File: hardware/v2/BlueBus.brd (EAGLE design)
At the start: 95 x 65 mm, 150 parts, among them J1 TC2030, Q1 NMOSFET-BSS138K, Q2 PMOSFET-DMP32D4SSOT323, Q3 NMOSFET-BSS138K

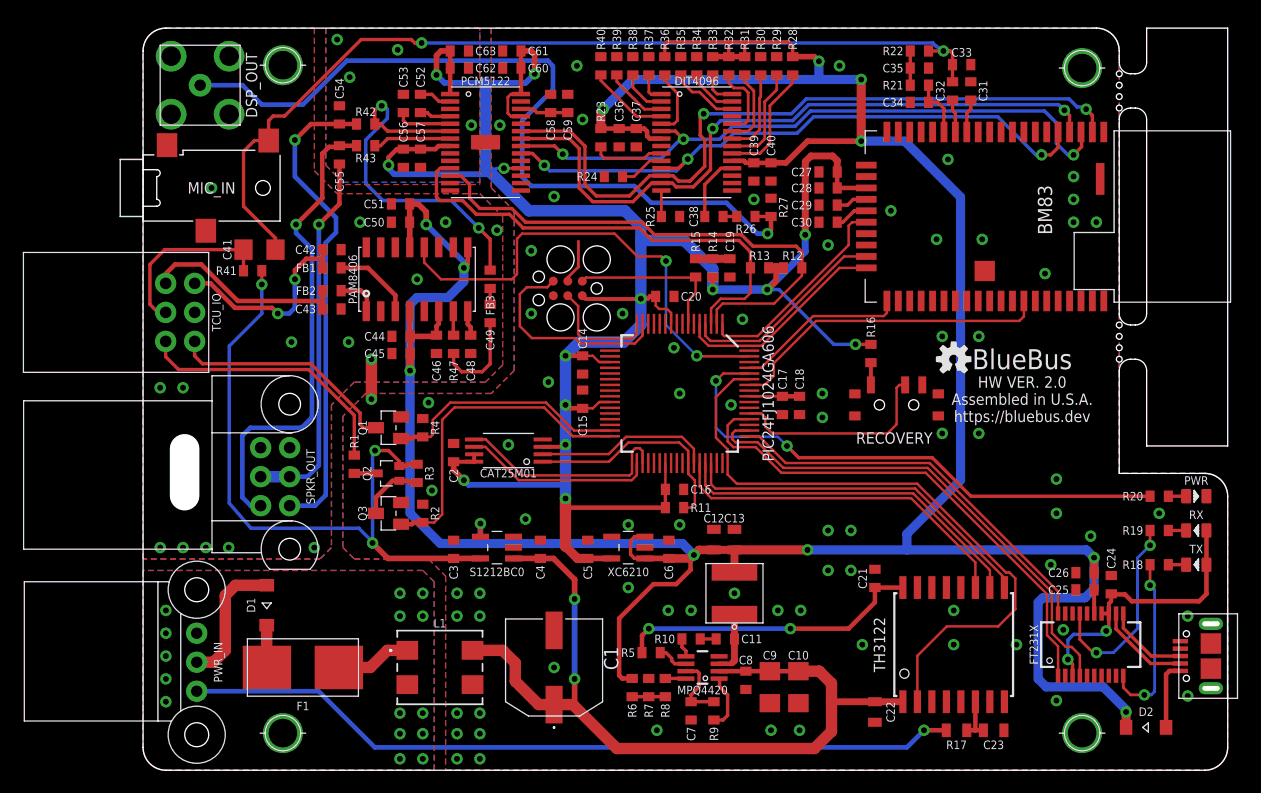
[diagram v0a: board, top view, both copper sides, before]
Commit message: [IMP] hardware: V2 Improvements * Increase the footprint for C1 and fix the name location * Remove PU/PD resistors from DIT4096 * Rewire I2S lines * Fix ground pour polygon dimensions * Replace 10ohm resistor for two parallel 20ohm * Wire SMB ground to unfiltered ground * Rename all connectors and ICs per convention * Increase name size to 1mm at minimum * Add additional ground VIAs
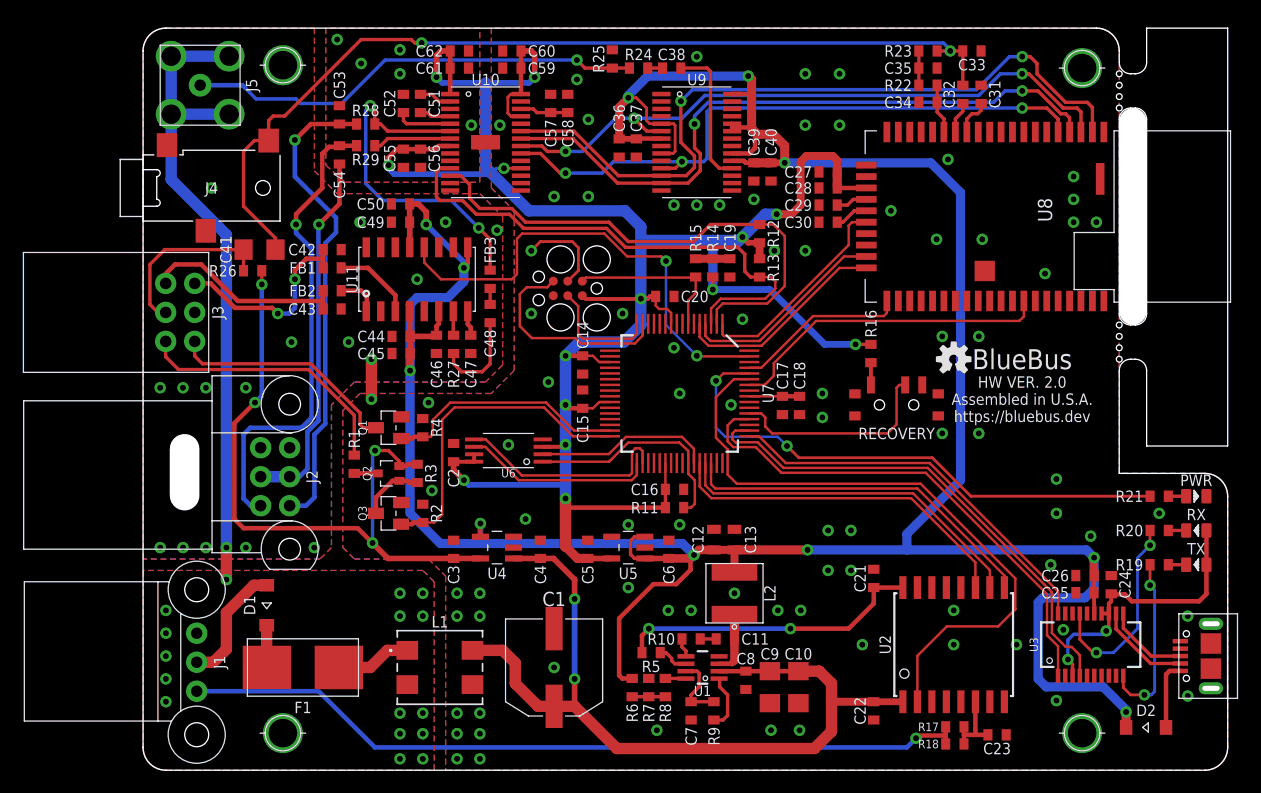
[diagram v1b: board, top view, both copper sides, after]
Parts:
- removed C63: 10uF, Passives:0603
- removed PWR_IN: 3PIN_953442_1, Connectors:TE_MQS_3PIN
- removed R30, R31, R32, R33, R34, R35, R36, R37, R38, R39, R40: 4.7k, Passives:0603
- removed R41: 10k, Passives:0603
- removed R42, R43: 100, Passives:0603
- removed R47: 18k, Passives:0603
- added C47: 1uF, Passives:0603
- added J8: TC2030, Connectors:TC2030
- C22: device Passives:0805 -> Passives:0603
- C23: value 100PF -> 100pF; device Passives:0805 -> Passives:0603
- C50: value 1uF -> 10uF
- C51: value 10uF -> 2.2uF
- C53: value 2.2uF -> 10nF
- C55: value 10nF -> 0.1uF
- C56, C60, C62: value 0.1uF -> 10uF
- C58, C61: value 10uF -> 0.1uF
- J1: value TC2030 -> 3PIN_953442_1; device Connectors:TC2030 -> Connectors:TE_MQS_3PIN
- R17: value 10 -> 20; device Passives:0805 -> Passives:0603
- R18: value 2k -> 20
- R21: value 1k -> 2k
- R23: value 4.7k -> 1k
- R24, R25: value 4.7k -> 150
- R26: value 150 -> 10k
- R27: value 150 -> 18k
- R28, R29: value 4.7k -> 100
- moved J1 44.4 mm to (4.70, 12.0), turned to 270 degrees
- moved R26 43.5 mm to (9.60, 43.8), turned to 180 degrees
- moved R21 41.7 mm to (89.0, 24.0), turned to 180 degrees
- moved R28 37.7 mm to (19.5, 56.6), turned to 180 degrees
- moved R29 36.7 mm to (19.5, 54.7), turned to 180 degrees
- moved R27 30.3 mm to (27.2, 37.3)
- moved R23 29.6 mm to (68.8, 63.0), turned to 180 degrees
- moved R18 23.8 mm to (71.1, 2.30), turned to 0 degrees
- moved R25 14.7 mm to (41.1, 62.3), turned to 90 degrees
- moved C38 13.5 mm to (46.3, 61.5), turned to 180 degrees
- moved C57 12.4 mm to (35.7, 58.4), turned to 90 degrees
- moved C49 11.2 mm to (22.6, 48.0), turned to 180 degrees
- moved R24 9.75 mm to (43.4, 61.5), turned to 180 degrees
- moved C51 8.97 mm to (24.3, 58.4), turned to 270 degrees
- moved C59 5.80 mm to (32.3, 61.5), turned to 180 degrees
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- renumbered BM83 to U8, CAT25M01 to U6, DIT4096 to U9, DSP_OUT to J5, FT231X to U3, MIC_IN to J4, MPQ4420 to U1, PAM8406 to U11, PCM5122 to U10, PIC24FJ1024GA606 to U7, RECOVERY to J7, S1212BC0 to U4, SPKR_OUT to J2, TCU_IO to J3, TH3122 to U2, USB to J6, XC6210 to U5
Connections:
- removed net SPDIF_AUDIO: R30.2, U9.22
- removed net SPDIF_BLSM: R32.1, U9.24
- removed net SPDIF_CLK0: R36.2, U9.5
- removed net SPDIF_CLK1: R40.2, U9.4
- removed net SPDIF_COPY: R38.2, U9.2
- removed net SPDIF_CSS: R37.1, U9.1
- removed net SPDIF_EMPH: R31.1, U9.23
- removed net SPDIF_FMT0: R23.2, U9.9
- removed net SPDIF_FMT1: R24.2, U9.10
- removed net SPDIF_L: R39.2, U9.3
- removed net SPDIF_MDAT: R28.1, U9.20
- removed net SPDIF_MODE: R33.2, U9.28
- removed net SPDIF_MONO: R29.1, U9.21
- removed net SPDIF_MS: R25.1, U9.14
- removed net SPDIF_U: R34.2, U9.27
- removed net SPDIF_V: R35.2, U9.26
- net 12V: now also R26.1; no longer R41.1
- net 3.3V: now also C55.1, C59.1, J8.2; no longer C57.1, C63.1, J1.2
- net 5V: now also C49.1, U9.20, U9.23, U9.24, U9.28, U9.5, U9.9; no longer C51.1, R23.1, R28.2, R31.2, R32.2, R33.1, R36.1
- net AGND: now also C52.1, C53.2, C61.2; no longer C53.1, C57.2, C63.2
- net BT_MIC_L: now also R23.1; no longer R22.1
- net DAC_CAPM: now also C51.2; no longer C52.2
- net DAC_CAPP: now also C51.1; no longer C52.1
- net DAC_LDOO: now also C57.1; no longer C59.1
- net DAC_OUT_L: now also R28.1; no longer R42.1
- net DAC_OUT_R: now also R29.1; no longer R43.1
- net DAC_VNEG: now also C52.2; no longer C53.2
- net GND: now also C47.2, C49.2, C57.2, J7.4, J7.5, J7.6, J7.7, J8.3, U9.1, U9.10, U9.14, U9.2, U9.21, U9.22, U9.26, U9.27, U9.3, U9.4; no longer C48.2, C51.2, C61.2, J1.3, J5.1, J5.2, J5.3, J5.4, R24.1, R27.2, R29.2, R30.1, R34.1, R35.1, R37.2, R38.1, R39.1, R40.1
- net GND_FLT: now also J1.1, J5.1, J5.2, J5.3, J5.4; no longer PWR_IN.1
- net IBUS: now also J1.3, R18.1; no longer PWR_IN.3
- net IBUS_FILT: now also R18.2
- net MCU_MCLR: now also J8.1; no longer J1.1
- net MCU_ON_LED: now also R21.2; no longer R20.2
- net MCU_ON_LED_RES: now also R21.1; no longer R20.1
- net MCU_PGC: now also J8.5; no longer J1.5
- net MCU_PGD: now also J8.4; no longer J1.4
- net MICP1_RES: now also R22.1, R23.2; no longer R21.1, R22.2
- net MIC_BIAS: now also R22.2; no longer R21.2
- net SPDIF_OUT: now also R24.2, R25.1; no longer R26.2, R27.1
- net SPDIF_TX_RES: now also R24.1; no longer R26.1
- net SPKR_OUT_L: now also C53.1, R28.2; no longer C54.1, R42.2
- net SPKR_OUT_R: now also C54.1, R29.2; no longer C55.1, R43.2
- net SYS_RX_LED: now also R20.2; no longer R19.2
- net SYS_RX_LED_RES: now also R20.1; no longer R19.1
- net SYS_TX_LED: now also R19.2; no longer R18.2
- net SYS_TX_LED_RES: now also R19.1; no longer R18.1
- net TEL_AMP_IN: now also C48.1; no longer C49.1
- net TEL_AMP_INL: now also R27.2; no longer R47.2
- net TEL_AMP_INL_CAP_RES: now also C48.2, R27.1; no longer C49.2, R47.1
- net TEL_AMP_VREF: now also C47.1; no longer C48.1
- net TEL_MIC_L_OUT: now also R26.2; no longer R41.2
- net VBAT: now also J1.2; no longer PWR_IN.2
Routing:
- net GND_FLT: track 0.00 -> 58.0 mm, vias 15 -> 17
- net SPDIF_OUT: track 70.8 -> 40.1 mm
- net 5V: track 284.8 -> 269.4 mm, vias 12 -> 11
- net SPDIF_MDAT: track 10.5 -> 0.00 mm
- net SPDIF_MONO: track 9.15 -> 0.00 mm
- net SPDIF_AUDIO: track 7.56 -> 0.00 mm
- net SPDIF_CLK1: track 7.09 -> 0.00 mm
- net SPDIF_EMPH: track 6.87 -> 0.00 mm
- net SPDIF_TX_FLT: track 5.79 -> 12.6 mm
- net SPDIF_BLSM: track 6.72 -> 0.00 mm
- net SPDIF_FMT0: track 6.30 -> 0.00 mm
- net SPDIF_V: track 6.03 -> 0.00 mm
- net SPDIF_CLK0: track 5.99 -> 0.00 mm
- net SPDIF_L: track 5.50 -> 0.00 mm
- net SPDIF_U: track 4.40 -> 0.00 mm
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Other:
- outline, holes or cut-outs redrawn
- board text added: "RECOVERY"

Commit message: Stuff
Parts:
- U4: value S-1212BC0-M5T1U -> S-1212BC0-U5T1U; device ICs:SOT23-5 -> ICs:SOT-89-5
- moved R24 24.2 mm to (19.2, 61.8)
- moved C38 24.1 mm to (22.2, 61.8)
- moved R25 24.1 mm to (17.0, 62.5)
- moved R2 4.50 mm to (20.0, 22.5), turned to 90 degrees
- moved C10 3.44 mm to (59.4, 10.1), turned to 90 degrees
- moved C9 3.44 mm to (56.9, 10.1), turned to 90 degrees
- moved C8 2.56 mm to (54.8, 9.47), turned to 90 degrees
- moved C7 2.50 mm to (50.5, 5.20)
- moved R6 2.50 mm to (45.3, 7.24)
- moved R7 2.50 mm to (46.8, 7.24)
- moved R8 2.50 mm to (48.2, 7.24)
- moved R9 2.50 mm to (52.5, 5.20)
- moved U1 2.50 mm to (51.5, 9.00)
- moved R5 2.15 mm to (46.5, 9.50)
- moved Q3 1.50 mm to (23.0, 22.5), turned to 270 degrees
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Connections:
- net 12V: now also U4.4; no longer U4.5
- net 5V: now also U4.5; no longer U4.4
- net VIN: now also U4.3; no longer U4.1
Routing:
- net SPDIF_TX_FLT: track 12.6 -> 41.3 mm
- net SPDIF_OUT: track 40.1 -> 14.9 mm, vias 1 -> 0
- net GND: track 11.5 -> 31.5 mm, vias 100 -> 98
- net BT_MIC_L: track 82.5 -> 63.4 mm, vias 2 -> 1
- net 3.3V: track 205.2 -> 219.9 mm, vias 14 -> 13
- net TEL_AMP_SHDN: track 41.6 -> 33.8 mm, vias 2 -> 0
- net MCU_ON_LED: track 47.8 -> 42.0 mm
- net DAC_OUT_L: track 31.2 -> 36.3 mm
- net 12V: track 58.4 -> 54.0 mm, vias 4 -> 2
- net EE_SCK: track 16.7 -> 20.8 mm
- net SPKR_OUT_L: track 42.0 -> 38.5 mm
- net SYS_DTR: track 44.6 -> 41.3 mm, vias 0 -> 2
- net 5VREG_BS: track 1.67 -> 4.27 mm
- net MCU_TEL_MUTE: track 21.4 -> 19.3 mm
- net TEL_MUTE_IO: track 20.3 -> 22.2 mm
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
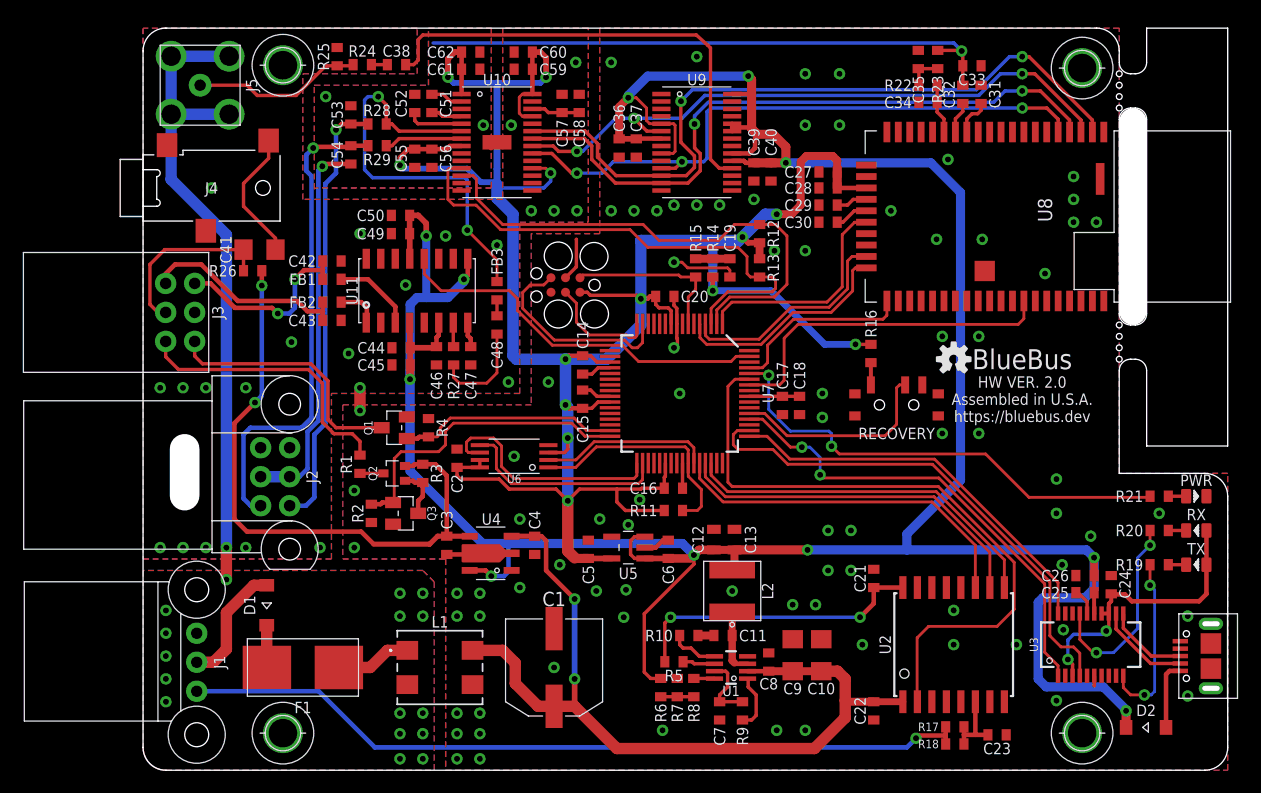
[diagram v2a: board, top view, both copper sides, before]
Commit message: [IMP] hardware: V2 Bugfixes and improvements Bug fixes:     * Wire floating S/PDIF reset pin to MCU     * Add pull up to MCU pin 64 for board identification Improvements:     * Added a 0.3mm isolation of the ground plane     * Switched by design rules to metric     * Moved the pin 1 indicators out from under the ICs to the side of pin 1     * Added outlines for all passives     * Moved over the impedance circuit for the S/PDIF output and kept the trace on the top layer     * Moved more traces off the bottom layer     * Moved the I2S lines to the top layer and reduced the VIA count from 11 to 5     * Revised all the packages in the design to ensure they matched the D/S. Specifically, the PIC24s package now has 0.3mm pads     * Set the minimum trace size to 0.25mm instead of 0.20mm     * Added more VIA floods for the ground plane to tie them together where the bottom layer gets bifurcated
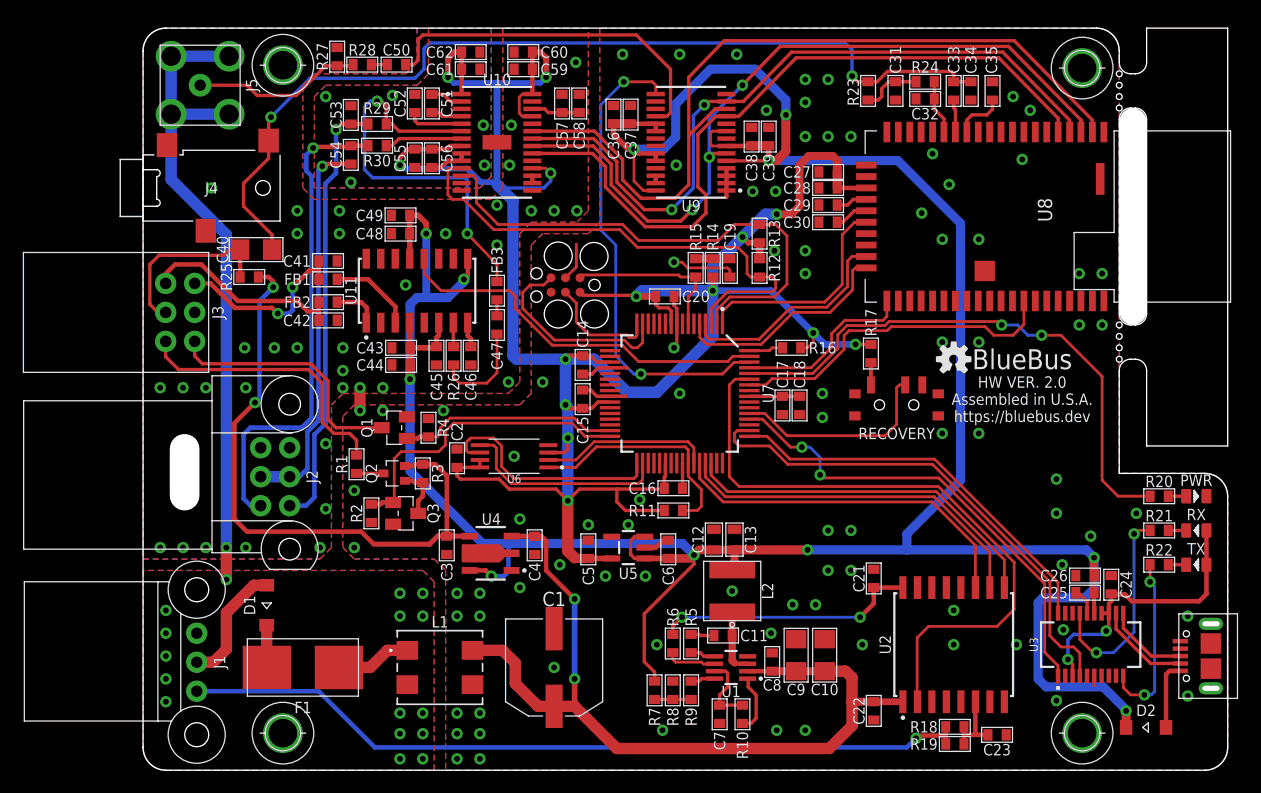
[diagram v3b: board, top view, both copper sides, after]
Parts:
- added R30: 100, Passives:0603
- C31, C32: value 47nF -> 1uF
- C33: value 200pF -> 47nF
- C34: value 1uF -> 200pF
- C35: value 1uF -> 47nF
- C36, C50: value 10uF -> 0.1uF
- C37: value 0.1uF -> 10uF
- C40: value 0.1uF -> 47UF1206; device Passives:0603 -> Passives:1206
- C41: value 47UF1206 -> 200pF; device Passives:1206 -> Passives:0603
- C43: value 200pF -> 10uF
- C44: value 10uF -> 1uF
- C49: value 1uF -> 10uF
- R10: value 20 -> 100k
- R17: value 20 -> 10k
- R19: value 2k -> 20
- R22: value 1k -> 2k
- R24: value 150 -> 1k
- R25: value 150 -> 10k
- R26: value 10k -> 18k
- R27: value 18k -> 150
- R28: value 100 -> 150
- R5: value 100k -> 20
- R6: value 41.2k -> 100k
- R7: value 7.68k -> 41.2k
- R8: value 51k -> 7.68k
- R9: value 100k -> 51k
- moved R24 49.3 mm to (68.5, 60.3), turned to 0 degrees
- moved R22 46.6 mm to (89.0, 18.0), turned to 180 degrees
- moved C40 45.6 mm to (9.90, 45.6), turned to 180 degrees
- moved R17 33.5 mm to (63.8, 36.5), turned to 90 degrees
- moved C38 31.7 mm to (53.3, 55.5), turned to 90 degrees
- moved R27 28.1 mm to (17.0, 62.5)
- moved R19 23.8 mm to (71.1, 2.30), turned to 0 degrees
- moved R25 20.8 mm to (9.30, 43.2), turned to 180 degrees
- moved R26 19.1 mm to (27.2, 36.3), turned to 90 degrees
- moved C50 13.2 mm to (22.2, 61.8)
- moved C48 11.6 mm to (22.6, 47.0), turned to 180 degrees
- moved R10 8.35 mm to (52.5, 4.90), turned to 90 degrees
- moved C31 7.51 mm to (65.9, 59.5)
- moved C35 7.06 mm to (74.4, 59.5), turned to 270 degrees
- moved R16 6.97 mm to (56.8, 37.0), turned to 0 degrees
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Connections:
- new net MCU_VER: R16.1, U7.64
- net 12V: now also R25.1; no longer R26.1
- net 3.3V: now also R17.2
- net 5V: now also C38.1, C43.1, C48.1, R7.2; no longer C40.1, C46.1, C50.1, R6.2
- net 5VREG_BS: now also R5.1; no longer R10.1
- net 5VREG_BS_CAP: now also R5.2; no longer R10.2
- net 5VREG_EN: now also R6.1; no longer R5.1
- net 5VREG_FB: now also R9.2; no longer R8.2
- net 5VREG_FB_T: now also R7.1, R8.2, R9.1; no longer R6.1, R7.2, R8.1
- net 5VREG_PG: now also R10.1; no longer R9.1
- net 5VREG_VCC: now also R10.2; no longer R9.2
- net BT_MIC_L: now also C34.1, C40.1; no longer C32.1, C41.1
- net DAC_OUT_L: now also R29.1; no longer R28.1
- net DAC_OUT_R: now also R30.1; no longer R29.1
- net GND: now also C31.2, C32.2, C35.1, C38.2, C41.2, C48.2, R27.2, R8.1; no longer C31.1, C33.2, C35.2, C40.2, C47.2, C50.2, R25.2, R7.1
- net IBUS: now also R19.1; no longer R17.1
- net IBUS_5V: now also R6.2; no longer R5.2
- net IBUS_FILT: now also R19.2; no longer R17.2
- net MCU_ON_LED: now also R20.2; no longer R21.2
- net MCU_ON_LED_RES: now also R20.1; no longer R21.1
- net MCU_SCK3: now also R13.1; no longer R12.1
- net MCU_SDA3: now also R12.1; no longer R13.1
- net MICN1: now also C35.2; no longer C31.2
- net MICP1: now also C33.2; no longer C32.2
- net MICP1_RES: now also C31.1, R24.1; no longer C35.1, R22.1
- net MIC_BIAS: now also C32.1, R24.2; no longer C34.1, R22.2
- net RECOVERY_ON: now also R17.1; no longer R16.1
- net SPDIF_OUT: now also R27.1, R28.2; no longer R24.2, R25.1
- net SPDIF_RST: now also U7.62
- net SPDIF_TX_FLT: now also C50.1; no longer C38.1
- net SPDIF_TX_RES: now also C50.2, R28.1; no longer C38.2, R24.1
- net SPKR_OUT_L: now also R29.2; no longer R28.2
- net SPKR_OUT_R: now also R30.2; no longer R29.2
- net SYS_RX_LED: now also R21.2; no longer R20.2
- net SYS_RX_LED_RES: now also R21.1; no longer R20.1
- net SYS_TX_LED: now also R22.2; no longer R19.2
- net SYS_TX_LED_RES: now also R22.1; no longer R19.1
- net TEL_AMP_IN: now also C47.1; no longer C48.1
- net TEL_AMP_INL: now also R26.2; no longer R27.2
- net TEL_AMP_INL_CAP_RES: now also C47.2, R26.1; no longer C48.2, R27.1
- net TEL_AMP_VREF: now also C46.1; no longer C47.1
- net TEL_MIC_L_OUT: now also C40.2, R25.2; no longer C41.2, R26.2
- net TEL_OUT_L+: now also C42.1; no longer C43.1
- net TEL_OUT_L-: now also C41.1; no longer C42.1
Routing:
- net SPDIF_RST: track 0.00 -> 41.9 mm, vias 0 -> 2
- net BT_MIC_L: track 63.4 -> 82.6 mm, vias 1 -> 2
- net I2S_CLK: track 56.7 -> 67.4 mm
- net SPDIF_TX_FLT: track 41.3 -> 31.8 mm
- net I2S_SCK: track 55.1 -> 64.4 mm, vias 3 -> 0
- net I2S_LRCK: track 64.1 -> 72.0 mm, vias 2 -> 0
- net MCU_ON_LED: track 42.0 -> 49.4 mm
- net 3.3V: track 219.9 -> 225.8 mm, vias 13 -> 14
- net I2S_DOUT: track 58.3 -> 63.7 mm
- net GND: track 31.5 -> 35.6 mm, vias 98 -> 123
- net AGND: track 34.2 -> 37.7 mm, vias 3 -> 6
- net IBUS_5V: track 26.4 -> 23.1 mm
- net MCU_VER: track 0.00 -> 3.00 mm
- net 5V: track 268.0 -> 270.2 mm
- net MICP1_RES: track 3.17 -> 5.27 mm
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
